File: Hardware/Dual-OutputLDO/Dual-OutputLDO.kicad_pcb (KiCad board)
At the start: 2 copper layers, 45 x 25 mm, 35 parts

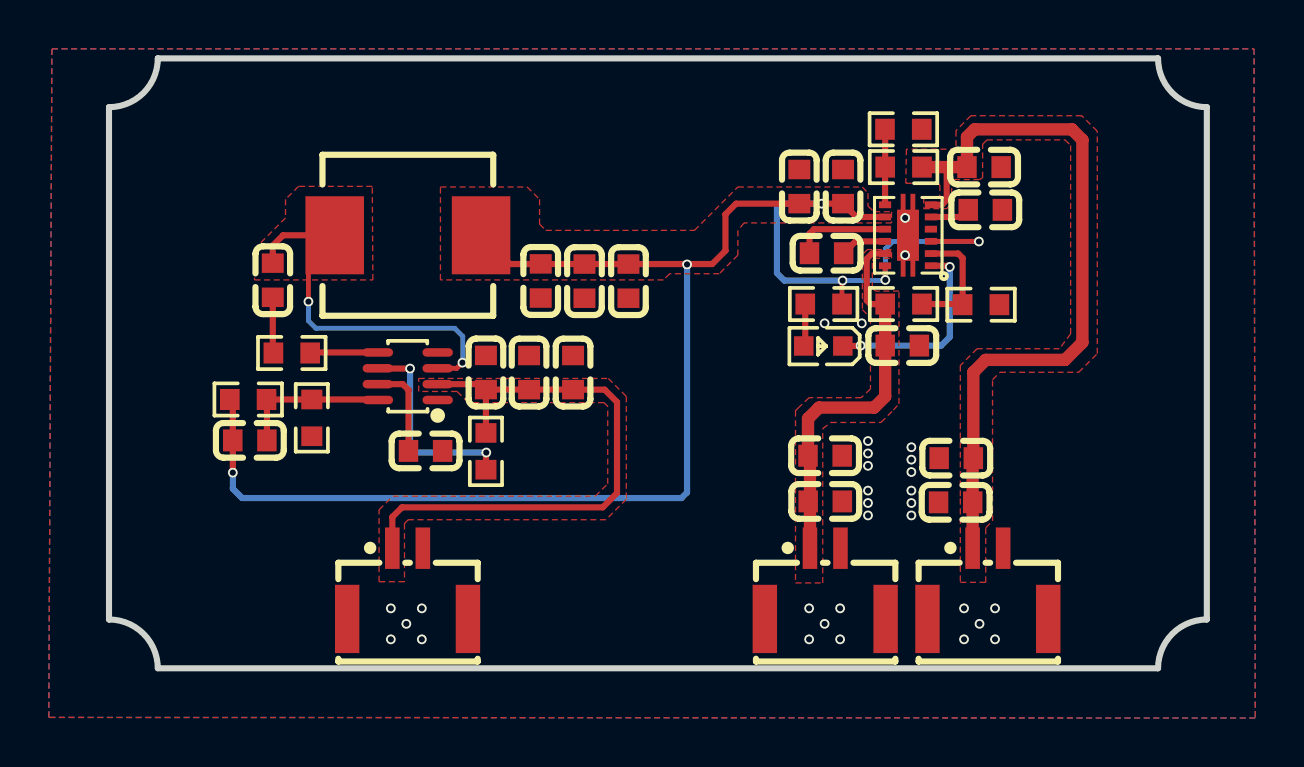
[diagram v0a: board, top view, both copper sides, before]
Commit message: complete Dual-OutputLDO
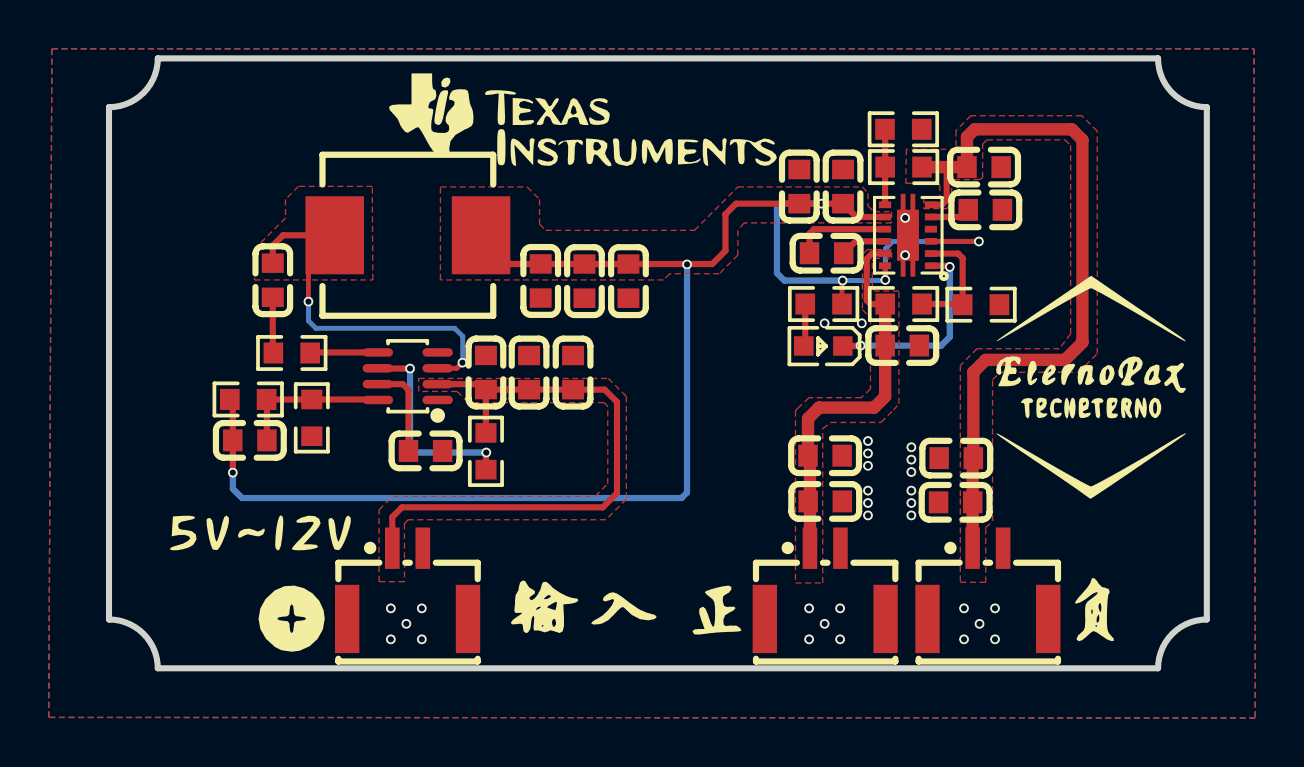
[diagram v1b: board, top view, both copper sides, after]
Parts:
- added G***: LOGO, Logo:logo_bottom, F.Cu at (104.6, 109.7)
- added G***: LOGO, Logo:logo_up, F.Cu at (103.9, 109.2)
